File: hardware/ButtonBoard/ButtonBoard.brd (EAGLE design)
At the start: 194.8 x 30.5 mm, 12 parts

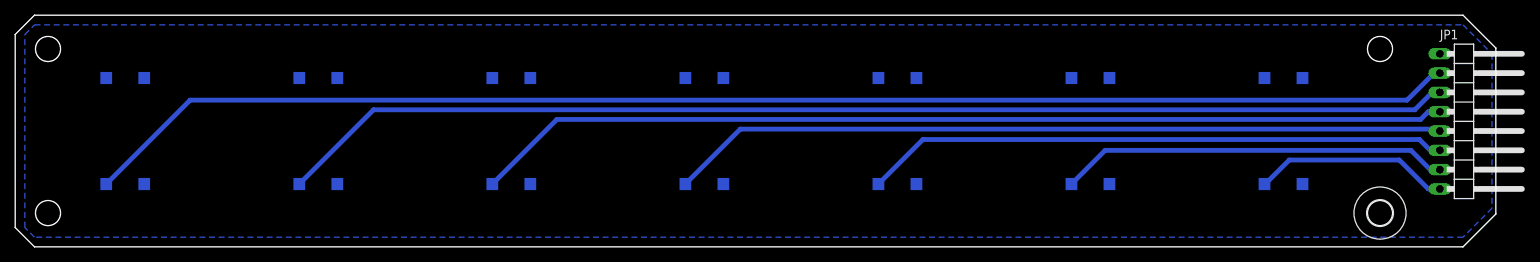
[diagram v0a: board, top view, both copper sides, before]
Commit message: increase mounting hole size
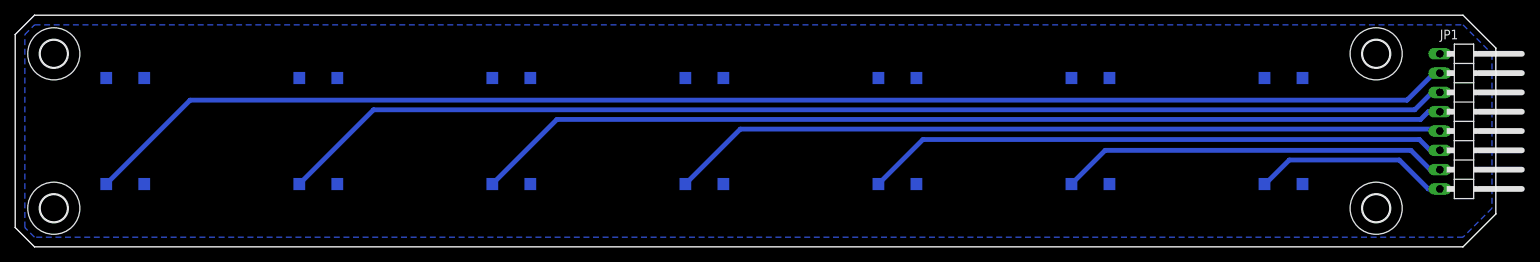
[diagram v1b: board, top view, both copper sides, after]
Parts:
- removed U$4: (no value), holes:3,3
- added U$5: (no value), holes:3,6
- U$1, U$2, U$3: device holes:3,3 -> holes:3,6
- moved U$2 174.8 mm to (179.1, 5.08), flipped to the top
- moved U$1 21.0 mm to (5.08, 5.08), flipped to the top
- moved U$3 0.81 mm to (179.1, 25.4), flipped to the top
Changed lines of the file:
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@@
 <attribute name="VALUE" x="173.101" y="15.24" size="0.6096" layer="28" font="vector" ratio="20" rot="MR270" align="top-center"/>
 </element>
-<element name="U$1" library="holes" library_urn="urn:adsk.eagle:library:237" package="3,3" package3d_urn="urn:adsk.eagle:package:14278/1" value="" x="4.318" y="26.035" smashed="yes" rot="MR0"/>
-<element name="U$2" library="holes" library_urn="urn:adsk.eagle:library:237" package="3,3" package3d_urn="urn:adsk.eagle:package:14278/1" value="" x="4.318" y="4.445" smashed="yes" rot="MR0"/>
-<element name="U$3" library="holes" library_urn="urn:adsk.eagle:library:237" package="3,3" package3d_urn="urn:adsk.eagle:package:14278/1" value="" x="179.578" y="26.035" smashed="yes" rot="MR0"/>
-<element name="U$4" library="holes" library_urn="urn:adsk.eagle:library:237" package="3,3" package3d_urn="urn:adsk.eagle:package:14278/1" value="" x="179.578" y="4.445" smashed="yes"/>
+<element name="U$5" library="holes" library_urn="urn:adsk.eagle:library:237" package="3,6" package3d_urn="urn:adsk.eagle:package:14272/1" value="" x="5.08" y="25.4" smashed="yes"/>
+<element name="U$1" library="holes" library_urn="urn:adsk.eagle:library:237" package="3,6" package3d_urn="urn:adsk.eagle:package:14272/1" value="" x="5.08" y="5.08" smashed="yes"/>
+<element name="U$2" library="holes" library_urn="urn:adsk.eagle:library:237" package="3,6" package3d_urn="urn:adsk.eagle:package:14272/1" value="" x="179.07" y="5.08" smashed="yes"/>
+<element name="U$3" library="holes" library_urn="urn:adsk.eagle:library:237" package="3,6" package3d_urn="urn:adsk.eagle:package:14272/1" value="" x="179.07" y="25.4" smashed="yes"/>
 </elements>
 <signals>
